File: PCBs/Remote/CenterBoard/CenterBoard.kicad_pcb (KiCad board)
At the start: 2 copper layers, 100 x 100 mm, 61 parts, among them J201 DX07S016JA1R1500, J801 SMA-RP, U101 Sparkfun_COM-09032, U102 Sparkfun_COM-09032, U201 LPC51U68JBD64, U401 SC189ZSKTRT, U801 nRF24L01P, U802 RFX2401C, X801 16MHz

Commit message: Bezig met LEDS
Signed-off-by: Eldalote.Electronics <Eldalote.Electronics@gmail.com>
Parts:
- removed C801: 33nF, Capacitor_SMD:C_0402_1005Metric
- removed C802: 1nF, Capacitor_SMD:C_0402_1005Metric
- removed C803, C811: 10nF, Capacitor_SMD:C_0402_1005Metric
- removed C804, C805: 15pF, Capacitor_SMD:C_0402_1005Metric
- removed C806: 2.2nF, Capacitor_SMD:C_0402_1005Metric
- removed C807: 1.5pF, Capacitor_SMD:C_0402_1005Metric
- removed C808: 4.7pF, Capacitor_SMD:C_0402_1005Metric
- removed C809: 1.0pF, Capacitor_SMD:C_0402_1005Metric
- removed C810: 220pF, Capacitor_SMD:C_0402_1005Metric
- removed C812: 1uF, Capacitor_SMD:C_0402_1005Metric
- removed C813: 0.3pF, Capacitor_SMD:C_0603_1608Metric
- removed C814, C815, C816, C817: 1pF, Capacitor_SMD:C_0402_1005Metric
- removed J801: SMA-RP, Connector_Coaxial:SMA_Samtec_SMA-J-P-X-ST-EM1_EdgeMount
- removed L801: 8.2nH, Inductor_SMD:L_0402_1005Metric
- removed L802, L804, L805: 2.7nH, Inductor_SMD:L_0402_1005Metric
- removed L803: 3.9nH, Inductor_SMD:L_0402_1005Metric
- removed LOGO1: Logo_Open_Hardware_Small, Symbol:OSHW-Logo_5.7x6mm_SilkScreen
- removed R801: 22K, Resistor_SMD:R_0402_1005Metric
- removed R802, R803: 1K, Resistor_SMD:R_0402_1005Metric
- removed R804: 2K, Resistor_SMD:R_0402_1005Metric
- removed U801: nRF24L01P, Package_DFN_QFN:QFN-20-1EP_4x4mm_P0.5mm_EP2.5x2.5mm
- removed U802: RFX2401C, SamacSys_Parts:QFN50P300X300X60-17N-D
- removed X801: 16MHz, Crystal:Crystal_SMD_3225-4Pin_3.2x2.5mm
- added C301: 10uF, Capacitor_SMD:C_0805_2012Metric_Pad1.15x1.40mm_HandSolder, F.Cu at (209.2, 126.9)
- added C302: 22uF, Capacitor_SMD:C_0805_2012Metric_Pad1.15x1.40mm_HandSolder, F.Cu at (214.4, 122.3)
- added C402: 1nF, Capacitor_SMD:C_0402_1005Metric, F.Cu at (266.0, 109.0)
- added C403: 10nF, Capacitor_SMD:C_0402_1005Metric, F.Cu at (271.1, 102.7)
- added C405: 15pF, Capacitor_SMD:C_0402_1005Metric, F.Cu at (257.3, 111.4)
- added C406: 2.2nF, Capacitor_SMD:C_0402_1005Metric, F.Cu at (266.5, 107.0)
- added C407: 1.5pF, Capacitor_SMD:C_0603_1608Metric_Pad1.05x0.95mm_HandSolder, F.Cu at (269.5, 98.4)
- added C408: 1.0pF, Capacitor_SMD:C_0603_1608Metric_Pad1.05x0.95mm_HandSolder, F.Cu at (258.0, 109.1)
- added C409: 4.7pF, Capacitor_SMD:C_0402_1005Metric, F.Cu at (269.4, 107.0)
- added C410: 220pF, Capacitor_SMD:C_0402_1005Metric, F.Cu at (271.7, 100.7)
- added C411: 10nF, Capacitor_SMD:C_0402_1005Metric, F.Cu at (273.1, 98.2)
- added C412: 1uF, Capacitor_SMD:C_0402_1005Metric, F.Cu at (268.8, 100.7)
- added C413: 0.3pF, Capacitor_SMD:C_0603_1608Metric_Pad1.05x0.95mm_HandSolder, F.Cu at (264.2, 103.7)
- added FL401: 2450LP14A100T, SamacSys_Parts:2450LP14A100T, F.Cu at (268.1, 104.2)
- added J401: SMA, Connector_Coaxial:SMA_Samtec_SMA-J-P-X-ST-EM1_EdgeMount, F.Cu at (251.2, 100.5)
- added L301: 1uH, Eldalote-footprints:L_3012_TDK, F.Cu at (214.3, 126.0)
- added L402: 2.7nH, Inductor_SMD:L_0402_1005Metric, F.Cu at (260.2, 111.4)
- added L403: 3.9nH, Inductor_SMD:L_0402_1005Metric, F.Cu at (272.4, 106.6)
- added LOGO101: Logo_Open_Hardware_Small, Symbol:OSHW-Logo_5.7x6mm_SilkScreen, F.Cu at (195.9, 155.9)
- added R401: 22K, Resistor_SMD:R_0402_1005Metric, F.Cu at (268.9, 109.0)
- added R402: 1K, Resistor_SMD:R_0402_1005Metric, F.Cu at (266.0, 111.0)
- added R403: 1K, Resistor_SMD:R_0402_1005Metric, F.Cu at (271.1, 104.6)
- added U301: SC189ZSKTRT, SamacSys_Parts:SOT95P280X145-5N, F.Cu at (209.4, 123.1)
- added U402: RFX2401C, Package_DFN_QFN:QFN-16-1EP_3x3mm_P0.5mm_EP1.75x1.75mm, F.Cu at (264.7, 99.8)
- added X401: 16MHz, Crystal:Crystal_SMD_3225-4Pin_3.2x2.5mm, F.Cu at (258.4, 105.6)
- C401: value 10uF -> 33nF; footprint Capacitor_SMD:C_0805_2012Metric_Pad1.15x1.40mm_HandSolder -> Capacitor_SMD:C_0603_1608Metric
- C404: value 22uF -> 15pF; footprint Capacitor_SMD:C_0805_2012Metric_Pad1.15x1.40mm_HandSolder -> Capacitor_SMD:C_0402_1005Metric
- L401: value 1uH -> 8.2nH; footprint Eldalote-footprints:L_3012_TDK -> Inductor_SMD:L_0402_1005Metric
- R201, R202: footprint Resistor_SMD:R_0805_2012Metric_Pad1.15x1.40mm_HandSolder -> Resistor_SMD:R_0603_1608Metric_Pad1.05x0.95mm_HandSolder; moved to B.Cu
- R203, R204, R205, R206: footprint Resistor_SMD:R_0805_2012Metric_Pad1.15x1.40mm_HandSolder -> Resistor_SMD:R_0603_1608Metric_Pad1.05x0.95mm_HandSolder
- S201, S202, U201: moved to B.Cu
- U401: value SC189ZSKTRT -> nRF24L01P; footprint SamacSys_Parts:SOT95P280X145-5N -> Eldalote-footprints:nRF24L01P-QFN-20-1EP_4x4mm_P0.5mm_EP
- moved R202 133.7 mm to (152.9, 150.3), turned to 270 degrees
- moved R201 127.6 mm to (151.4, 150.3), turned to 270 degrees
- moved U201 110.2 mm to (150.0, 110.0), turned to 90 degrees
- moved S201 101.6 mm to (143.0, 128.4), turned to 90 degrees
- moved S202 92.5 mm to (158.3, 122.0), turned to 270 degrees
- moved R204 66.0 mm to (206.3, 99.0)
- moved C205 65.0 mm to (209.2, 116.0)
- moved C204 62.5 mm to (214.0, 113.1)
- moved C207 62.5 mm to (214.0, 116.0)
- moved C212 58.2 mm to (223.5, 115.1)
- moved R206 51.0 mm to (232.4, 114.9)
- moved C206 49.1 mm to (218.7, 115.1)
- moved C209 45.2 mm to (233.9, 101.6)
- moved C203 42.0 mm to (233.9, 98.6)
- moved C401 37.9 mm to (263.1, 106.2)
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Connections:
- C401 pad 1: +5V -> Net-(C401-Pad1)
- C404 pad 1: +3V3 -> GND
- C404 pad 2: GND -> Net-(C404-Pad2)
- L401 pad 1: /Power/3v3_LX -> Net-(L401-Pad1)
- L401 pad 2: +3V3 -> Net-(L401-Pad2)
- U401 pad 1: +5V -> nRF_CE
- U401 pad 2: GND -> nRF_CSn
- U401 pad 3: +5V -> nRF_SCLK
- U401 pad 4: +3V3 -> nRF_MOSI
- U401 pad 5: /Power/3v3_LX -> nRF_MISO
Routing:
- net Net-(J201-Pad5): track 0.00 -> 5.98 mm
- net Net-(J201-Pad6): track 0.00 -> 4.46 mm

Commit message: Continued work with the center board
Signed-off-by: Eldalote.Electronics <Eldalote.Electronics@gmail.com>
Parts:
- removed R101: PTA6043, Eldalote-footprints:PTA6043
- removed U101, U102: Sparkfun_COM-09032, Eldalote-footprints:Sparkfun_COM-09032
- added C214: 100nF, Capacitor_SMD:C_0402_1005Metric, B.Cu at (131.7, 103.5)
- added D501: LED_POWERGOOD, LED_SMD:LED_0805_2012Metric_Pad1.15x1.40mm_HandSolder, F.Cu at (76.4, 82.7)
- added D502: LED_ERROR, LED_SMD:LED_0805_2012Metric_Pad1.15x1.40mm_HandSolder, F.Cu at (76.4, 79.7)
- added D503: RGB User LED, digikey-footprints:6-PLCC_3.5x3.5mm, F.Cu at (70.6, 81.0)
- added D504: LED_POWERGOOD, LED_SMD:LED_0805_2012Metric_Pad1.15x1.40mm_HandSolder, F.Cu at (69.7, 85.4)
- added D505: LED_POWERGOOD, LED_SMD:LED_0805_2012Metric_Pad1.15x1.40mm_HandSolder, F.Cu at (54.9, 97.5)
- added D506: LED_POWERGOOD, LED_SMD:LED_0805_2012Metric_Pad1.15x1.40mm_HandSolder, F.Cu at (54.9, 100.5)
- added D507: LED_POWERGOOD, LED_SMD:LED_0805_2012Metric_Pad1.15x1.40mm_HandSolder, F.Cu at (54.9, 103.6)
- added J501: Conn_01x11, Connector_PinHeader_2.54mm:PinHeader_1x11_P2.54mm_Vertical_SMD_Pin1Left, F.Cu at (166.2, 85.3)
- added POT501: Screen brightness Potentiometer, digikey-footprints:Potentiometer_P120PK-Y25BR10K, F.Cu at (182.8, 78.5)
- added R501: 560R, Resistor_SMD:R_0402_1005Metric, F.Cu at (68.7, 90.4)
- added R502: 560R, Resistor_SMD:R_0402_1005Metric, F.Cu at (58.8, 99.5)
- added R503: 30R, Resistor_SMD:R_0603_1608Metric_Pad1.05x0.95mm_HandSolder, F.Cu at (80.9, 79.4)
- added R504: 240R, Resistor_SMD:R_0603_1608Metric_Pad1.05x0.95mm_HandSolder, F.Cu at (69.4, 88.1)
- added R505: 240R, Resistor_SMD:R_0603_1608Metric_Pad1.05x0.95mm_HandSolder, F.Cu at (59.5, 97.2)
- added R506: 560R, Resistor_SMD:R_0402_1005Metric, F.Cu at (73.5, 85.2)
- added R507: 560R, Resistor_SMD:R_0402_1005Metric, F.Cu at (58.8, 101.5)
- added R508: 560R, Resistor_SMD:R_0402_1005Metric, F.Cu at (63.1, 97.0)
- added R509: 560R, Resistor_SMD:R_0402_1005Metric, F.Cu at (54.0, 106.1)
- added R601: Throttle Potentiometer, Eldalote-footprints:PTA6043, F.Cu at (106.3, 109.8)
- added R602: 10k, Resistor_SMD:R_0805_2012Metric_Pad1.15x1.40mm_HandSolder, B.Cu at (118.1, 111.8)
- added R603: 10k, Resistor_SMD:R_0805_2012Metric_Pad1.15x1.40mm_HandSolder, B.Cu at (177.7, 111.0)
- added U202: W25Q128JVS, Package_SO:SOIC-8_5.23x5.23mm_P1.27mm, B.Cu at (125.9, 101.5)
- added U601: Joystick Left, Eldalote-footprints:Sparkfun_COM-09032, F.Cu at (126.0, 125.4)
- added U602: Joystick Right, Eldalote-footprints:Sparkfun_COM-09032, F.Cu at (185.8, 124.5)
- C401, C402, C403, C404, C405, C406, C407, C408, C409, C410, C411, C412, C413, FL401, J401, L401, L402, L403, R401, R402, R403, U401, U402, X401: moved to B.Cu
- moved R403 128.8 mm to (146.8, 70.8)
- moved C409 126.1 mm to (147.4, 75.4), turned to 270 degrees
- moved R402 125.5 mm to (146.8, 71.7)
- moved L403 124.4 mm to (152.1, 74.9)
- moved C406 124.3 mm to (146.3, 75.4), turned to 270 degrees
- moved FL401 124.2 mm to (150.0, 65.8), turned to 90 degrees
- moved C410 122.1 mm to (153.1, 71.3), turned to 90 degrees
- moved C411 121.9 mm to (154.2, 71.3), turned to 90 degrees
- moved C404 120.7 mm to (145.8, 81.9), turned to 180 degrees
- moved C413 120.6 mm to (149.1, 67.6)
- moved C407 120.4 mm to (151.7, 73.6)
- moved R401 119.9 mm to (153.5, 76.5), turned to 90 degrees
- moved C403 118.6 mm to (155.0, 78.7), turned to 90 degrees
- moved U402 118.1 mm to (150.2, 70.7), turned to 90 degrees
- moved C405 117.6 mm to (144.9, 76.6)
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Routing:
- net GND: track 0.00 -> 31.2 mm
- net +3V3: track 0.00 -> 15.2 mm
- net /Radio/VDD_PA: track 0.00 -> 12.2 mm
- net Net-(C404-Pad2): track 0.00 -> 6.34 mm
- net Net-(C405-Pad2): track 0.00 -> 4.35 mm
- net Net-(L401-Pad1): track 0.00 -> 3.45 mm
- net Net-(FL401-Pad5): track 0.00 -> 3.45 mm
- net Net-(L401-Pad2): track 0.00 -> 3.44 mm
- net Net-(C407-Pad1): track 0.00 -> 3.16 mm
- net Net-(C413-Pad2): track 0.00 -> 3.12 mm
- net Net-(C401-Pad1): track 0.00 -> 2.20 mm
- net nRF_IRQ: track 0.00 -> 2.18 mm
- net Net-(R401-Pad1): track 0.00 -> 2.06 mm
- net /Radio/RXEN: track 0.00 -> 1.56 mm
- net /Radio/TXEN: track 0.00 -> 1.36 mm
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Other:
- copper layers 2 -> 4

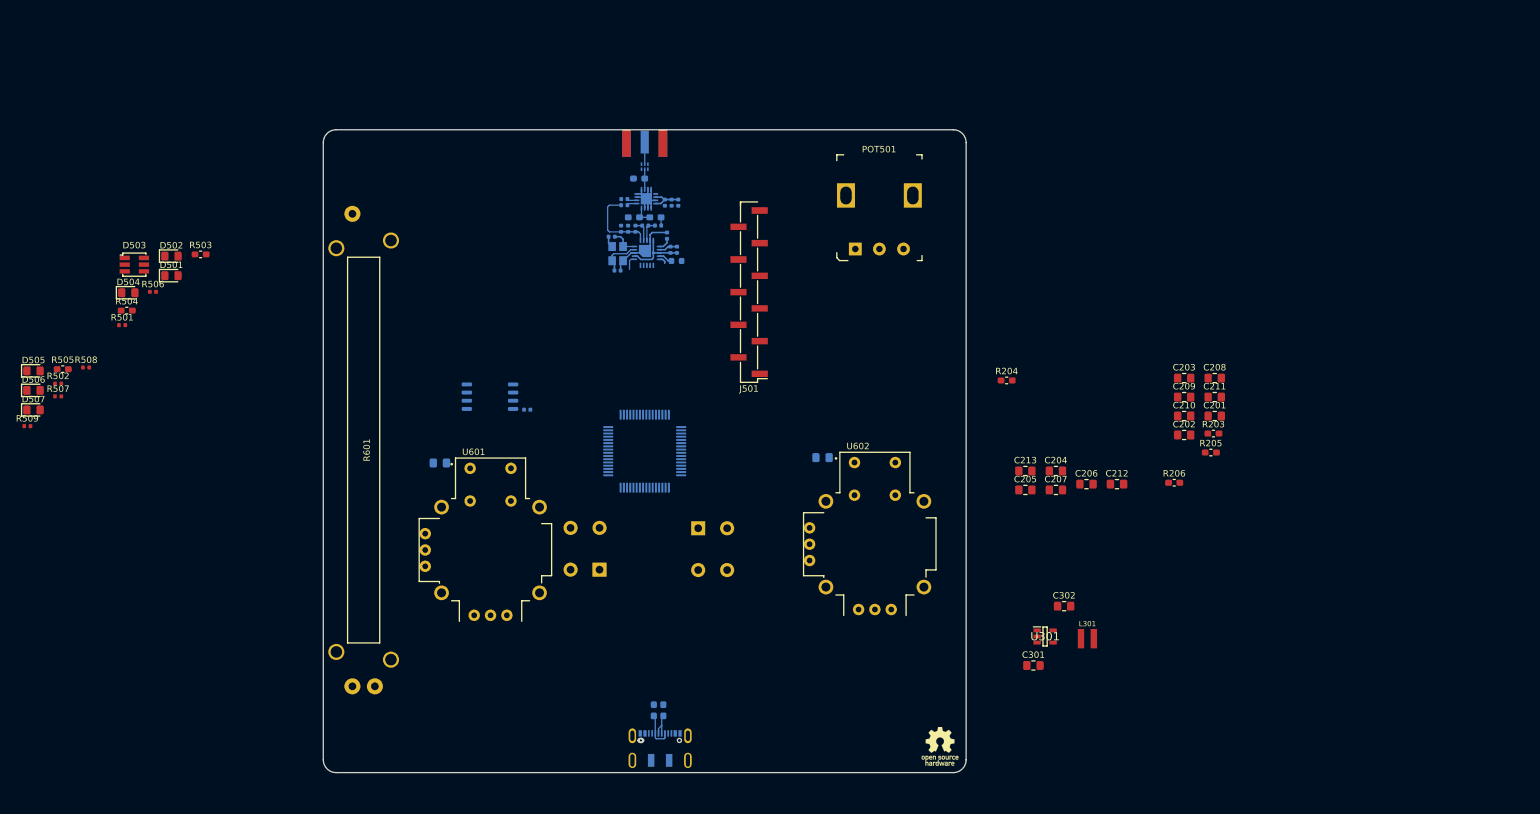
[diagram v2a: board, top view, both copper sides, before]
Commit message: Note: Schmitt trigger for joystick Buttons TODO
Signed-off-by: Eldalote.Electronics <Eldalote.Electronics@gmail.com>
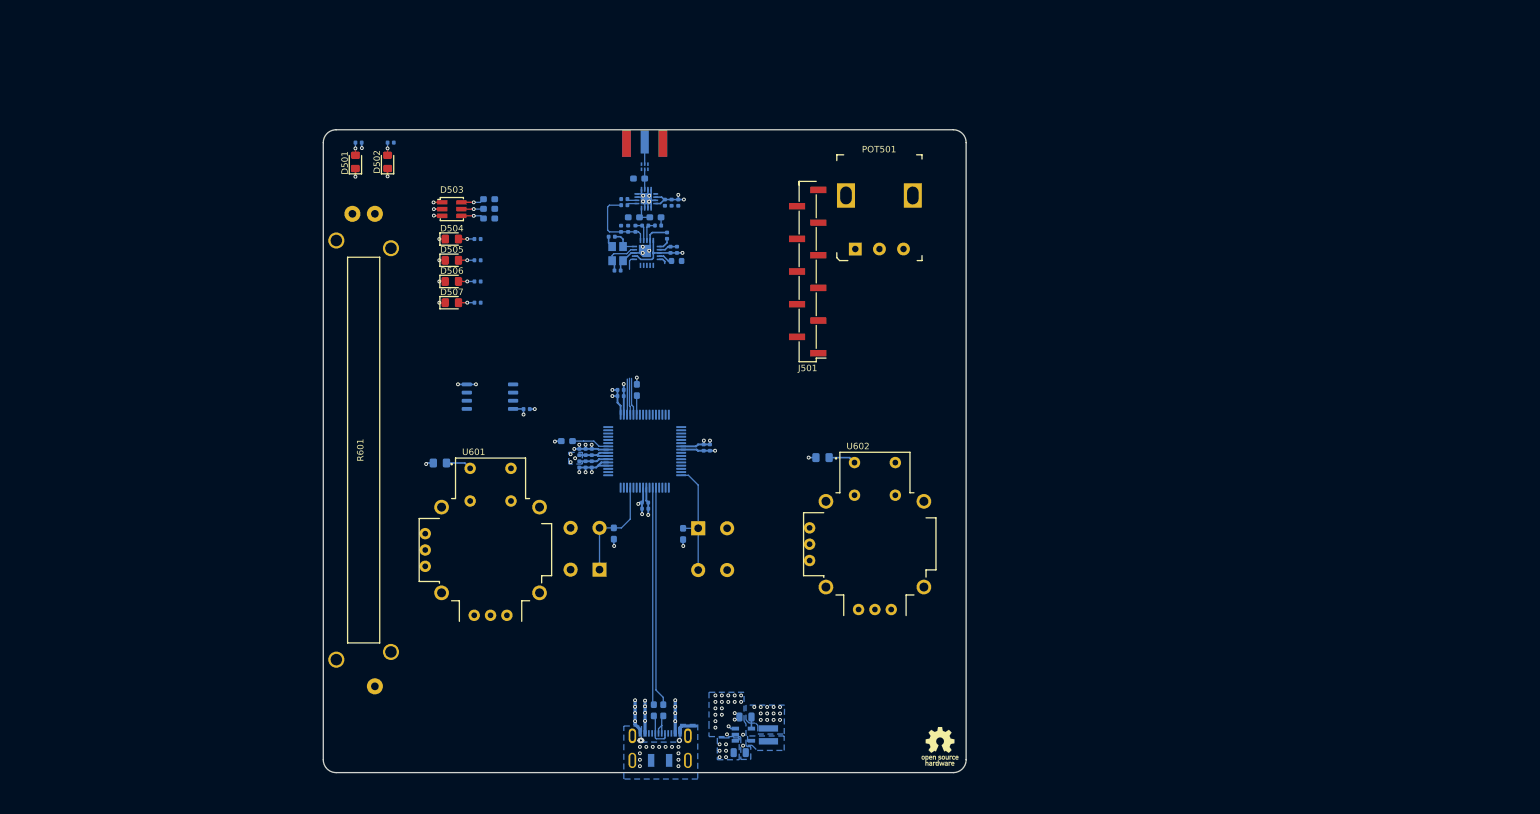
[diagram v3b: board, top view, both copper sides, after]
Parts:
- removed C202: 100nF, Capacitor_SMD:C_0805_2012Metric_Pad1.15x1.40mm_HandSolder
- C201, C203, C204, C205, C206, C207, C208, C209, C210, C211, C212, C213: footprint Capacitor_SMD:C_0805_2012Metric_Pad1.15x1.40mm_HandSolder -> Capacitor_SMD:C_0402_1005Metric; moved to B.Cu
- C301, C302: footprint Capacitor_SMD:C_0805_2012Metric_Pad1.15x1.40mm_HandSolder -> Capacitor_SMD:C_0805_2012Metric; moved to B.Cu
- D504: value LED_POWERGOOD -> LED_USER_0
- D505: value LED_POWERGOOD -> LED_USER_1
- D506: value LED_POWERGOOD -> LED_USER_2
- D507: value LED_POWERGOOD -> LED_USER_3
- L301, R203, R204, R205, R206, R501, R502, R503, R504, R505, R506, R507, R508, R509, U301: moved to B.Cu
- moved C208 98.5 mm to (140.8, 110.1), turned to 90 degrees
- moved C201 97.2 mm to (141.8, 112.0), turned to 270 degrees
- moved C203 95.0 mm to (139.8, 112.0), turned to 270 degrees
- moved R206 94.7 mm to (137.9, 108.4)
- moved R203 94.6 mm to (145.2, 122.8), turned to 90 degrees
- moved C209 92.5 mm to (141.8, 110.1), turned to 90 degrees
- moved C211 92.4 mm to (146.2, 101.4), turned to 180 degrees
- moved C210 87.8 mm to (146.3, 100.5), turned to 180 degrees
- moved R205 83.1 mm to (156.0, 122.9), turned to 90 degrees
- moved C204 74.2 mm to (139.8, 110.1), turned to 90 degrees
- moved R509 72.6 mm to (124.0, 86.9)
- moved R505 70.3 mm to (125.8, 73.8), turned to 180 degrees
- moved C206 68.8 mm to (150.1, 119.0), turned to 180 degrees
- moved R507 68.6 mm to (124.0, 80.3)
- moved C205 68.5 mm to (140.8, 112.0), turned to 270 degrees
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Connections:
- net Net-(U202-Pad1) renamed /LPC51/Flash_SPI_CSn
- net Net-(U202-Pad6) renamed /LPC51/Flash_SPI_SCLK
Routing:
- net GND: track 31.2 -> 87.2 mm, vias 0 -> 70
- net +3V3: track 15.2 -> 54.8 mm, vias 0 -> 30
- net /LPC51/USB_DP: track 0.00 -> 34.2 mm
- net /LPC51/USB_DM: track 0.00 -> 33.8 mm
- net /LPC51/RESET: track 0.00 -> 18.8 mm
- net /LPC51/ISP0: track 0.00 -> 16.7 mm
- net +5V: track 0.00 -> 11.4 mm, vias 0 -> 15
- net /LPC51/ISP-VBUS: track 0.00 -> 5.89 mm
- net Net-(U201-Pad37): track 0.00 -> 5.77 mm
- net Net-(U201-Pad36): track 0.00 -> 5.72 mm
- net Net-(U201-Pad35): track 0.00 -> 5.56 mm
- net JS_right_button: track 0.00 -> 4.27 mm
- net JS_left_button: track 0.00 -> 4.02 mm
- net Net-(D503-Pad6): track 0.00 -> 3.63 mm, vias 0 -> 1
- net Net-(D503-Pad4): track 0.00 -> 3.59 mm, vias 0 -> 1
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- added copper zone on B.Cu, net +3V3
- added copper zone on In2.Cu, net +3V3
- added copper zone on B.Cu, net +5V
- added copper zone on In2.Cu, net +5V
- added copper zone on B.Cu, net /Power/3v3_LX
- added copper zone on B.Cu, net GND
- added copper zone on In1.Cu, net GND
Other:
- board text added: "Program"
- board text added: "Reset"
